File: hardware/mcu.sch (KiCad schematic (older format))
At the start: 22 parts, among them P3 SWD, P4 SPI3, P5 UART5, P7 USB_B, SW1 RESET, SW2 BOOT, U5 STM32F405R, U7 USBUFxxW6, X1 8MHz

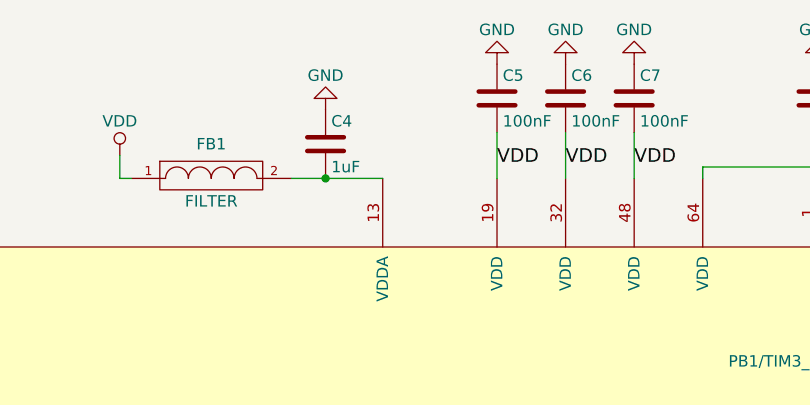
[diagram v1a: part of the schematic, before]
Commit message: Preliminary routing with LTC4417
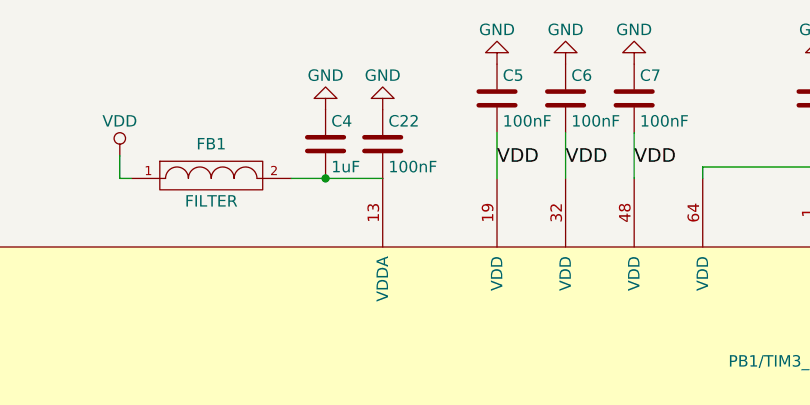
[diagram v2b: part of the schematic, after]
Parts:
- added C22: 100nF, Capacitors_SMD:C_0805, symbol C
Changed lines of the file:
@@
 EESchema Schematic File Version 2
+LIBS:rgb-matrix-rescue
 LIBS:power
 LIBS:device
@@
 $EndDescr
 $Comp
-L GND #PWR010
+L GND #PWR011
 U 1 1 580FD53D
 P 3800 5950
-F 0 "#PWR010" H 3800 5700 50  0001 C CNN
+F 0 "#PWR011" H 3800 5700 50  0001 C CNN
 F 1 "GND" H 3800 5800 50  0000 C CNN
 F 2 "" H 3800 5950 50  0000 C CNN
@@
 $EndComp
 $Comp
-L GND #PWR011
+L GND #PWR012
 U 1 1 580FFFC5
 P 4400 750
-F 0 "#PWR011" H 4400 500 50  0001 C CNN
+F 0 "#PWR012" H 4400 500 50  0001 C CNN
 F 1 "GND" H 4400 600 50  0000 C CNN
 F 2 "" H 4400 750 50  0000 C CNN
@@
 $EndComp
 $Comp
-L GND #PWR012
+L GND #PWR013
 U 1 1 58100274
 P 4700 750
-F 0 "#PWR012" H 4700 500 50  0001 C CNN
+F 0 "#PWR013" H 4700 500 50  0001 C CNN
 F 1 "GND" H 4700 600 50  0000 C CNN
 F 2 "" H 4700 750 50  0000 C CNN
@@
 $EndComp
 $Comp
-L GND #PWR013
+L GND #PWR014
 U 1 1 581002A9
 P 5000 750
-F 0 "#PWR013" H 5000 500 50  0001 C CNN
+F 0 "#PWR014" H 5000 500 50  0001 C CNN
 F 1 "GND" H 5000 600 50  0000 C CNN
 F 2 "" H 5000 750 50  0000 C CNN
@@
 $EndComp
 $Comp
-L GND #PWR014
+L GND #PWR015
 U 1 1 58100346
 P 5800 750
-F 0 "#PWR014" H 5800 500 50  0001 C CNN
+F 0 "#PWR015" H 5800 500 50  0001 C CNN
 F 1 "GND" H 5800 600 50  0000 C CNN
 F 2 "" H 5800 750 50  0000 C CNN
@@
 $EndComp
 $Comp
-L GND #PWR015
+L GND #PWR016
 U 1 1 58100502
 P 900 2450
-F 0 "#PWR015" H 900 2200 50  0001 C CNN
+F 0 "#PWR016" H 900 2200 50  0001 C CNN
 F 1 "GND" H 900 2300 50  0000 C CNN
 F 2 "" H 900 2450 50  0000 C CNN
@@
 $EndComp
 $Comp
-L GND #PWR016
+L GND #PWR017
 U 1 1 5810057A
 P 3650 950
-F 0 "#PWR016" H 3650 700 50  0001 C CNN
+F 0 "#PWR017" H 3650 700 50  0001 C CNN
 F 1 "GND" H 3650 800 50  0000 C CNN
 F 2 "" H 3650 950 50  0000 C CNN
@@
 $EndComp
 $Comp
-L VDD #PWR017
+L VDD #PWR018
 U 1 1 581006D5
 P 2750 1150
-F 0 "#PWR017" H 2750 1000 50  0001 C CNN
+F 0 "#PWR018" H 2750 1000 50  0001 C CNN
 F 1 "VDD" H 2750 1300 50  0000 C CNN
 F 2 "" H 2750 1150 50  0000 C CNN
@@
 $EndComp
 $Comp
-L GND #PWR018
+L GND #PWR019
 U 1 1 581008E0
 P 4000 5950
-F 0 "#PWR018" H 4000 5700 50  0001 C CNN
+F 0 "#PWR019" H 4000 5700 50  0001 C CNN
 F 1 "GND" H 4000 5800 50  0000 C CNN
 F 2 "" H 4000 5950 50  0000 C CNN
@@
 $EndComp
 $Comp
-L GND #PWR019
+L GND #PWR020
 U 1 1 58100906
 P 4200 5950
-F 0 "#PWR019" H 4200 5700 50  0001 C CNN
+F 0 "#PWR020" H 4200 5700 50  0001 C CNN
 F 1 "GND" H 4200 5800 50  0000 C CNN
 F 2 "" H 4200 5950 50  0000 C CNN
@@
 $EndComp
 $Comp
-L GND #PWR020
+L GND #PWR021
 U 1 1 58100A18
 P 5100 6250
-F 0 "#PWR020" H 5100 6000 50  0001 C CNN
+F 0 "#PWR021" H 5100 6000 50  0001 C CNN
 F 1 "GND" H 5100 6100 50  0000 C CNN
 F 2 "" H 5100 6250 50  0000 C CNN
@@
 $EndComp
 $Comp
-L GND #PWR021
+L GND #PWR022
 U 1 1 58100A9B
 P 5600 6250
-F 0 "#PWR021" H 5600 6000 50  0001 C CNN
+F 0 "#PWR022" H 5600 6000 50  0001 C CNN
 F 1 "GND" H 5600 6100 50  0000 C CNN
 F 2 "" H 5600 6250 50  0000 C CNN
@@
 $EndComp
 $Comp
-L GND #PWR022
+L GND #PWR023
 U 1 1 581010C3
 P 900 3050
-F 0 "#PWR022" H 900 2800 50  0001 C CNN
+F 0 "#PWR023" H 900 2800 50  0001 C CNN
 F 1 "GND" H 900 2900 50  0000 C CNN
 F 2 "" H 900 3050 50  0000 C CNN
@@
 NRST
 $Comp
-L GND #PWR023
+L GND #PWR024
 U 1 1 58102147
 P 1050 7500
-F 0 "#PWR023" H 1050 7250 50  0001 C CNN
+F 0 "#PWR024" H 1050 7250 50  0001 C CNN
 F 1 "GND" H 1050 7350 50  0000 C CNN
 F 2 "" H 1050 7500 50  0000 C CNN
@@
 BOOT1
 $Comp
-L GND #PWR024
+L GND #PWR025
 U 1 1 5815BDE6
 P 1950 7550
-F 0 "#PWR024" H 1950 7300 50  0001 C CNN
+F 0 "#PWR025" H 1950 7300 50  0001 C CNN
 F 1 "GND" H 1950 7400 50  0000 C CNN
 F 2 "" H 1950 7550 50  0000 C CNN
@@
 BOOT0
 $Comp
-L VDD #PWR025
+L VDD #PWR026
 U 1 1 5815C70B
 P 1950 6300
-F 0 "#PWR025" H 1950 6150 50  0001 C CNN
+F 0 "#PWR026" H 1950 6150 50  0001 C CNN
 F 1 "VDD" H 1950 6450 50  0000 C CNN
 F 2 "" H 1950 6300 50  0000 C CNN
@@
 $EndComp
 $Comp
-L VDD #PWR026
+L VDD #PWR027
 U 1 1 5815F752
 P 1050 6450
-F 0 "#PWR026" H 1050 6300 50  0001 C CNN
+F 0 "#PWR027" H 1050 6300 50  0001 C CNN
 F 1 "VDD" H 1050 6600 50  0000 C CNN
 F 2 "" H 1050 6450 50  0000 C CNN
@@
 SPI3_NSS
 $Comp
-L GND #PWR027
+L GND #PWR028
 U 1 1 581B0CAC
 P 10650 4600
-F 0 "#PWR027" H 10650 4350 50  0001 C CNN
+F 0 "#PWR028" H 10650 4350 50  0001 C CNN
 F 1 "GND" H 10650 4450 50  0000 C CNN
 F 2 "" H 10650 4600 50  0000 C CNN
@@
 $EndComp
 $Comp
-L +5V #PWR028
+L +5V #PWR029
 U 1 1 581B0D1D
 P 10650 4100
-F 0 "#PWR028" H 10650 3950 50  0001 C CNN
+F 0 "#PWR029" H 10650 3950 50  0001 C CNN
 F 1 "+5V" H 10650 4240 50  0000 C CNN
 F 2 "" H 10650 4100 50  0000 C CNN
@@
 $EndComp
 $Comp
-L GND #PWR029
+L GND #PWR030
 U 1 1 581C3953
 P 10650 5400
-F 0 "#PWR029" H 10650 5150 50  0001 C CNN
+F 0 "#PWR030" H 10650 5150 50  0001 C CNN
 F 1 "GND" H 10650 5250 50  0000 C CNN
 F 2 "" H 10650 5400 50  0000 C CNN
@@
 $EndComp
 $Comp
-L +5V #PWR030
+L +5V #PWR031
 U 1 1 581C3C79
 P 10200 5600
-F 0 "#PWR030" H 10200 5450 50  0001 C CNN
+F 0 "#PWR031" H 10200 5450 50  0001 C CNN
 F 1 "+5V" H 10200 5740 50  0000 C CNN
 F 2 "" H 10200 5600 50  0000 C CNN
@@
 $EndComp
 $Comp
-L GND #PWR031
+L GND #PWR032
 U 1 1 582B947A
 P 8650 1050
-F 0 "#PWR031" H 8650 800 50  0001 C CNN
+F 0 "#PWR032" H 8650 800 50  0001 C CNN
 F 1 "GND" H 8650 900 50  0000 C CNN
 F 2 "" H 8650 1050 50  0000 C CNN
@@
 U 1 1 582B9480
 P 10750 950
+AR Path="/582B9480" Ref="P7"  Part="1"
+AR Path="/580FBD10/582B9480" Ref="P7"  Part="1"
 F 0 "P7" V 10450 850 50  0000 C CNN
 F 1 "USB_B" H 10700 1150 50  0000 C CNN
@@
 $EndComp
 $Comp
-L GND #PWR032
+L GND #PWR033
 U 1 1 582B9487
 P 10450 1400
-F 0 "#PWR032" H 10450 1150 50  0001 C CNN
+F 0 "#PWR033" H 10450 1150 50  0001 C CNN
 F 1 "GND" H 10450 1250 50  0000 C CNN
 F 2 "" H 10450 1400 50  0000 C CNN
@@
 $EndComp
 $Comp
-L +3V3 #PWR033
+L +3V3 #PWR034
 U 1 1 582B948D
 P 10100 1050
-F 0 "#PWR033" H 10100 900 50  0001 C CNN
+F 0 "#PWR034" H 10100 900 50  0001 C CNN
 F 1 "+3V3" H 10100 1190 50  0000 C CNN
 F 2 "" H 10100 1050 50  0000 C CNN
@@
 	10850 1350 10450 1350
 Connection ~ 10450 1350
+$Comp
+L C C22
+U 1 1 587848A6
+P 3900 1100
+F 0 "C22" H 3925 1200 50  0000 L CNN
+F 1 "100nF" H 3925 1000 50  0000 L CNN
+F 2 "Capacitors_SMD:C_0805" H 3938 950 50  0001 C CNN
+F 3 "" H 3900 1100 50  0000 C CNN
+	1    3900 1100
+	1    0    0    -1
+$EndComp
+$Comp
+L GND #PWR035
+U 1 1 58784915
+P 3900 950
+F 0 "#PWR035" H 3900 700 50  0001 C CNN
+F 1 "GND" H 3900 800 50  0000 C CNN
+F 2 "" H 3900 950 50  0000 C CNN
+F 3 "" H 3900 950 50  0000 C CNN
+	1    3900 950
+	-1   0    0    1
+$EndComp
 $EndSCHEMATC

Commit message: Fix silkscreen
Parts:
- C1, C10, C11, C2, C22, C3, C4, C5, C6, C7, C8: footprint Capacitors_SMD:C_0805 -> rgb-matrix:C_0805
- FB1, R26, R27: footprint Resistors_SMD:R_0805 -> rgb-matrix:R_0805
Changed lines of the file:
@@
 F 0 "C5" H 4425 1000 50  0000 L CNN
 F 1 "100nF" H 4425 800 50  0000 L CNN
-F 2 "Capacitors_SMD:C_0805" H 4438 750 50  0001 C CNN
+F 2 "rgb-matrix:C_0805" H 4438 750 50  0001 C CNN
 F 3 "" H 4400 900 50  0000 C CNN
 	1    4400 900
@@
 F 0 "C6" H 4725 1000 50  0000 L CNN
 F 1 "100nF" H 4725 800 50  0000 L CNN
-F 2 "Capacitors_SMD:C_0805" H 4738 750 50  0001 C CNN
+F 2 "rgb-matrix:C_0805" H 4738 750 50  0001 C CNN
 F 3 "" H 4700 900 50  0000 C CNN
 	1    4700 900
@@
 F 0 "C7" H 5025 1000 50  0000 L CNN
 F 1 "100nF" H 5025 800 50  0000 L CNN
-F 2 "Capacitors_SMD:C_0805" H 5038 750 50  0001 C CNN
+F 2 "rgb-matrix:C_0805" H 5038 750 50  0001 C CNN
 F 3 "" H 5000 900 50  0000 C CNN
 	1    5000 900
@@
 F 0 "C11" H 5825 1000 50  0000 L CNN
 F 1 "100nF" H 5825 800 50  0000 L CNN
-F 2 "Capacitors_SMD:C_0805" H 5838 750 50  0001 C CNN
+F 2 "rgb-matrix:C_0805" H 5838 750 50  0001 C CNN
 F 3 "" H 5800 900 50  0000 C CNN
 	1    5800 900
@@
 F 0 "C2" H 1075 2550 50  0000 L CNN
 F 1 "18pF" H 1075 2350 50  0000 L CNN
-F 2 "Capacitors_SMD:C_0805" H 1088 2300 50  0001 C CNN
+F 2 "rgb-matrix:C_0805" H 1088 2300 50  0001 C CNN
 F 3 "" H 1050 2450 50  0000 C CNN
 	1    1050 2450
@@
 F 0 "C4" H 3675 1200 50  0000 L CNN
 F 1 "1uF" H 3675 1000 50  0000 L CNN
-F 2 "Capacitors_SMD:C_0805" H 3688 950 50  0001 C CNN
+F 2 "rgb-matrix:C_0805" H 3688 950 50  0001 C CNN
 F 3 "" H 3650 1100 50  0000 C CNN
 	1    3650 1100
@@
 F 0 "FB1" H 3150 1400 50  0000 C CNN
 F 1 "FILTER" H 3150 1150 50  0000 C CNN
-F 2 "Resistors_SMD:R_0805" H 3150 1250 50  0001 C CNN
+F 2 "rgb-matrix:R_0805" H 3150 1250 50  0001 C CNN
 F 3 "" H 3150 1250 50  0000 C CNN
 	1    3150 1250
@@
 F 0 "C8" H 5125 6200 50  0000 L CNN
 F 1 "2.2uF" H 5125 6000 50  0000 L CNN
-F 2 "Capacitors_SMD:C_0805" H 5138 5950 50  0001 C CNN
+F 2 "rgb-matrix:C_0805" H 5138 5950 50  0001 C CNN
 F 3 "" H 5100 6100 50  0000 C CNN
 	1    5100 6100
@@
 F 0 "C10" H 5625 6200 50  0000 L CNN
 F 1 "2.2uF" H 5625 6000 50  0000 L CNN
-F 2 "Capacitors_SMD:C_0805" H 5638 5950 50  0001 C CNN
+F 2 "rgb-matrix:C_0805" H 5638 5950 50  0001 C CNN
 F 3 "" H 5600 6100 50  0000 C CNN
 	1    5600 6100
@@
 F 0 "C3" H 1075 3150 50  0000 L CNN
 F 1 "18pF" H 1075 2950 50  0000 L CNN
-F 2 "Capacitors_SMD:C_0805" H 1088 2900 50  0001 C CNN
+F 2 "rgb-matrix:C_0805" H 1088 2900 50  0001 C CNN
 F 3 "" H 1050 3050 50  0000 C CNN
 	1    1050 3050
@@
 F 0 "R27" V 2030 7250 50  0000 C CNN
 F 1 "10k" V 1950 7250 50  0000 C CNN
-F 2 "Resistors_SMD:R_0805" V 1880 7250 50  0001 C CNN
+F 2 "rgb-matrix:R_0805" V 1880 7250 50  0001 C CNN
 F 3 "" H 1950 7250 50  0000 C CNN
 	1    1950 7250
@@
 F 0 "C1" H 925 7250 50  0000 L CNN
 F 1 "100nF" H 925 7050 50  0000 L CNN
-F 2 "Capacitors_SMD:C_0805" H 938 7000 50  0001 C CNN
+F 2 "rgb-matrix:C_0805" H 938 7000 50  0001 C CNN
 F 3 "" H 900 7150 50  0000 C CNN
 	1    900  7150
@@
 F 0 "R26" V 1130 6650 50  0000 C CNN
 F 1 "10k" V 1050 6650 50  0000 C CNN
-F 2 "Resistors_SMD:R_0805" V 980 6650 50  0001 C CNN
+F 2 "rgb-matrix:R_0805" V 980 6650 50  0001 C CNN
 F 3 "" H 1050 6650 50  0000 C CNN
 	1    1050 6650
@@
 Text GLabel 1200 4750 0    60   UnSpc ~ 0
 VBUS
-Wire Wire Line
-	8200 2150 8600 2150
-Wire Wire Line
-	1200 5050 600  5050
-Wire Wire Line
-	1200 4950 600  4950
-Wire Wire Line
-	8200 2250 8600 2250
-Wire Wire Line
-	1200 5150 600  5150
-Wire Wire Line
-	1200 5250 600  5250
-Wire Wire Line
-	10650 3400 10050 3400
-Wire Wire Line
-	10650 3300 10050 3300
-Wire Wire Line
-	10650 3200 10050 3200
-Wire Wire Line
-	10650 3100 10050 3100
-Wire Wire Line
-	10650 3000 10050 3000
-Wire Wire Line
-	10650 2900 10050 2900
-Wire Wire Line
-	1200 2900 1200 3050
-Wire Wire Line
-	1200 2450 1200 2600
-Wire Wire Line
-	900  7000 900  6850
-Connection ~ 1050 7450
-Wire Wire Line
-	900  7450 900  7300
-Wire Wire Line
-	1050 7450 1050 7500
-Wire Wire Line
-	900  7450 1200 7450
-Wire Wire Line
-	850  2250 1200 2250
-Wire Wire Line
-	850  2050 1200 2050
-Connection ~ 3650 1250
-Wire Wire Line
-	3500 1250 3900 1250
-Wire Wire Line
-	5800 1050 5800 1250
-Wire Wire Line
-	5000 1050 5000 1250
-Wire Wire Line
-	4700 1050 4700 1250
-Wire Wire Line
-	4400 1050 4400 1250
-Wire Wire Line
-	1600 7050 1950 7050
-Wire Wire Line
-	1950 6950 1950 7100
-Wire Wire Line
-	1950 6300 1950 6350
-Connection ~ 1950 7050
-Wire Wire Line
-	1050 6450 1050 6500
-Wire Wire Line
-	650  6850 1200 6850
-Connection ~ 900  6850
-Wire Wire Line
-	1050 6850 1050 6800
-Connection ~ 1050 6850
-Wire Wire Line
-	1950 7400 1950 7550
-Wire Wire Line
-	1600 7500 1950 7500
-Connection ~ 1950 7500
-Wire Wire Line
-	2750 1150 2750 1250
-Wire Wire Line
-	2750 1250 2800 1250
-Wire Wire Line
-	1200 4450 1200 4450
-Wire Wire Line
-	1200 4550 1200 4550
-Wire Wire Line
-	8200 4750 8700 4750
-Wire Wire Line
-	8200 4850 8700 4850
-Wire Wire Line
-	8200 4950 9250 4950
-Wire Wire Line
-	600  5350 1200 5350
-Wire Wire Line
-	10650 4200 10200 4200
-Wire Wire Line
-	10200 4300 10650 4300
-Wire Wire Line
-	10200 4400 10650 4400
-Wire Wire Line
-	10200 4500 10650 4500
-Wire Wire Line
-	750  3450 1200 3450
-Wire Wire Line
-	10650 5700 10200 5700
-Wire Wire Line
-	10200 5800 10650 5800
-Wire Wire Line
-	10200 5600 10650 5600
-Wire Wire Line
-	5800 1200 5300 1200
-Wire Wire Line
-	5300 1200 5300 1250
-Connection ~ 5800 1200
 Text Label 8700 1150 0    60   ~ 0
 USB_DM
@@
 VBUS
 NoConn ~ 10450 1050
-Wire Wire Line
-	10200 750  10450 750
-Wire Wire Line
-	10100 950  10450 950
-Wire Wire Line
-	10350 850  10450 850
-Wire Wire Line
-	10350 1150 10350 850
-Wire Wire Line
-	10350 1150 10100 1150
-Wire Wire Line
-	8650 1050 9100 1050
-Wire Wire Line
-	9100 950  8700 950
-Wire Wire Line
-	9100 1150 8700 1150
-Wire Wire Line
-	10450 1150 10450 1400
-Wire Wire Line
-	10850 1350 10450 1350
-Connection ~ 10450 1350
 $Comp
 L C C22
@@
 F 0 "C22" H 3925 1200 50  0000 L CNN
 F 1 "100nF" H 3925 1000 50  0000 L CNN
-F 2 "Capacitors_SMD:C_0805" H 3938 950 50  0001 C CNN
+F 2 "rgb-matrix:C_0805" H 3938 950 50  0001 C CNN
 F 3 "" H 3900 1100 50  0000 C CNN
 	1    3900 1100
@@
 	-1   0    0    1
 $EndComp
+Wire Wire Line
+	8200 2150 8600 2150
+Wire Wire Line
+	1200 5050 600  5050
+Wire Wire Line
+	1200 4950 600  4950
+Wire Wire Line
+	8200 2250 8600 2250
+Wire Wire Line
+	1200 5150 600  5150
+Wire Wire Line
+	1200 5250 600  5250
+Wire Wire Line
+	10650 3400 10050 3400
+Wire Wire Line
+	10650 3300 10050 3300
+Wire Wire Line
+	10650 3200 10050 3200
+Wire Wire Line
+	10650 3100 10050 3100
+Wire Wire Line
+	10650 3000 10050 3000
+Wire Wire Line
+	10650 2900 10050 2900
+Wire Wire Line
+	1200 2900 1200 3050
+Wire Wire Line
+	1200 2450 1200 2600
+Wire Wire Line
+	900  7000 900  6850
+Connection ~ 1050 7450
+Wire Wire Line
+	900  7450 900  7300
+Wire Wire Line
+	1050 7450 1050 7500
+Wire Wire Line
+	900  7450 1200 7450
+Wire Wire Line
+	850  2250 1200 2250
+Wire Wire Line
+	850  2050 1200 2050
+Connection ~ 3650 1250
+Wire Wire Line
+	3500 1250 3900 1250
+Wire Wire Line
+	5800 1050 5800 1250
+Wire Wire Line
+	5000 1050 5000 1250
+Wire Wire Line
+	4700 1050 4700 1250
+Wire Wire Line
+	4400 1050 4400 1250
+Wire Wire Line
+	1600 7050 1950 7050
+Wire Wire Line
+	1950 6950 1950 7100
+Wire Wire Line
+	1950 6300 1950 6350
+Connection ~ 1950 7050
+Wire Wire Line
+	1050 6450 1050 6500
+Wire Wire Line
+	650  6850 1200 6850
+Connection ~ 900  6850
+Wire Wire Line
+	1050 6850 1050 6800
+Connection ~ 1050 6850
+Wire Wire Line
+	1950 7400 1950 7550
+Wire Wire Line
+	1600 7500 1950 7500
+Connection ~ 1950 7500
+Wire Wire Line
+	2750 1150 2750 1250
+Wire Wire Line
+	2750 1250 2800 1250
+Wire Wire Line
+	1200 4450 1200 4450
+Wire Wire Line
+	1200 4550 1200 4550
+Wire Wire Line
+	8200 4750 8700 4750
+Wire Wire Line
+	8200 4850 8700 4850
+Wire Wire Line
+	8200 4950 9250 4950
+Wire Wire Line
+	600  5350 1200 5350
+Wire Wire Line
+	10650 4200 10200 4200
+Wire Wire Line
+	10200 4300 10650 4300
+Wire Wire Line
+	10200 4400 10650 4400
+Wire Wire Line
+	10200 4500 10650 4500
+Wire Wire Line
+	750  3450 1200 3450
+Wire Wire Line
+	10650 5700 10200 5700
+Wire Wire Line
+	10200 5800 10650 5800
+Wire Wire Line
+	10200 5600 10650 5600
+Wire Wire Line
+	5800 1200 5300 1200
+Wire Wire Line
+	5300 1200 5300 1250
+Connection ~ 5800 1200
+Wire Wire Line
+	10200 750  10450 750
+Wire Wire Line
+	10100 950  10450 950
+Wire Wire Line
+	10350 850  10450 850
+Wire Wire Line
+	10350 1150 10350 850
+Wire Wire Line
+	10350 1150 10100 1150
+Wire Wire Line
+	8650 1050 9100 1050
+Wire Wire Line
+	9100 950  8700 950
+Wire Wire Line
+	9100 1150 8700 1150
+Wire Wire Line
+	10450 1150 10450 1400
+Wire Wire Line
+	10850 1350 10450 1350
+Connection ~ 10450 1350
 $EndSCHEMATC

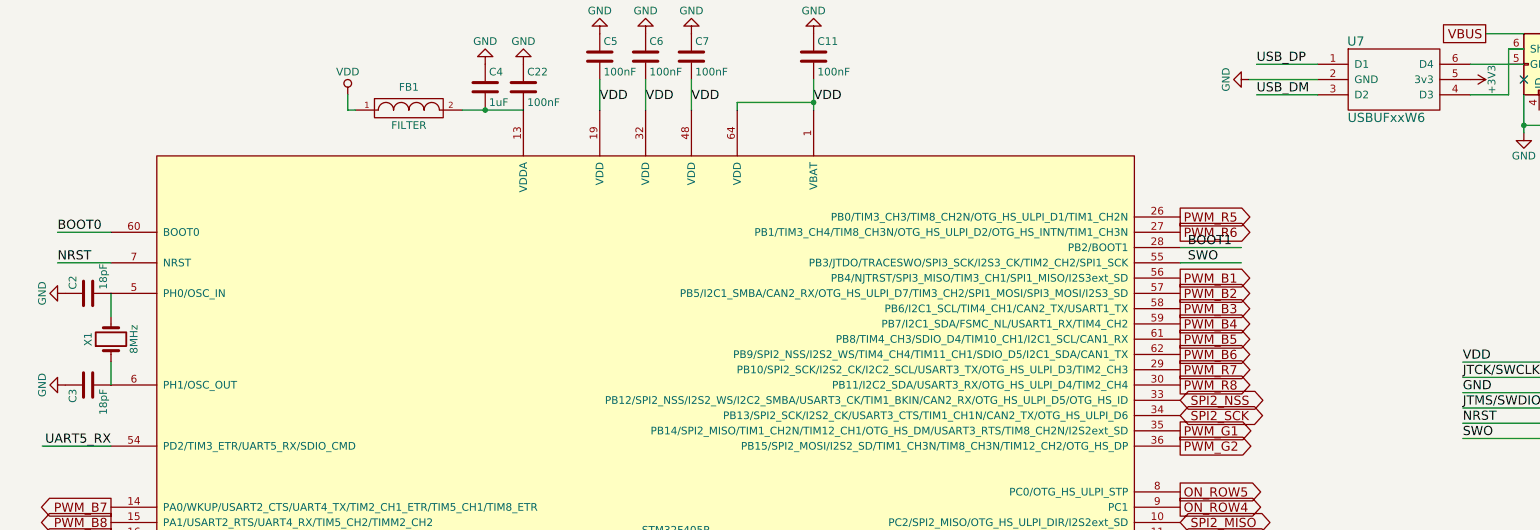
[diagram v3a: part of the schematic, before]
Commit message: Add 2nd GND pin for more curent + minor changes
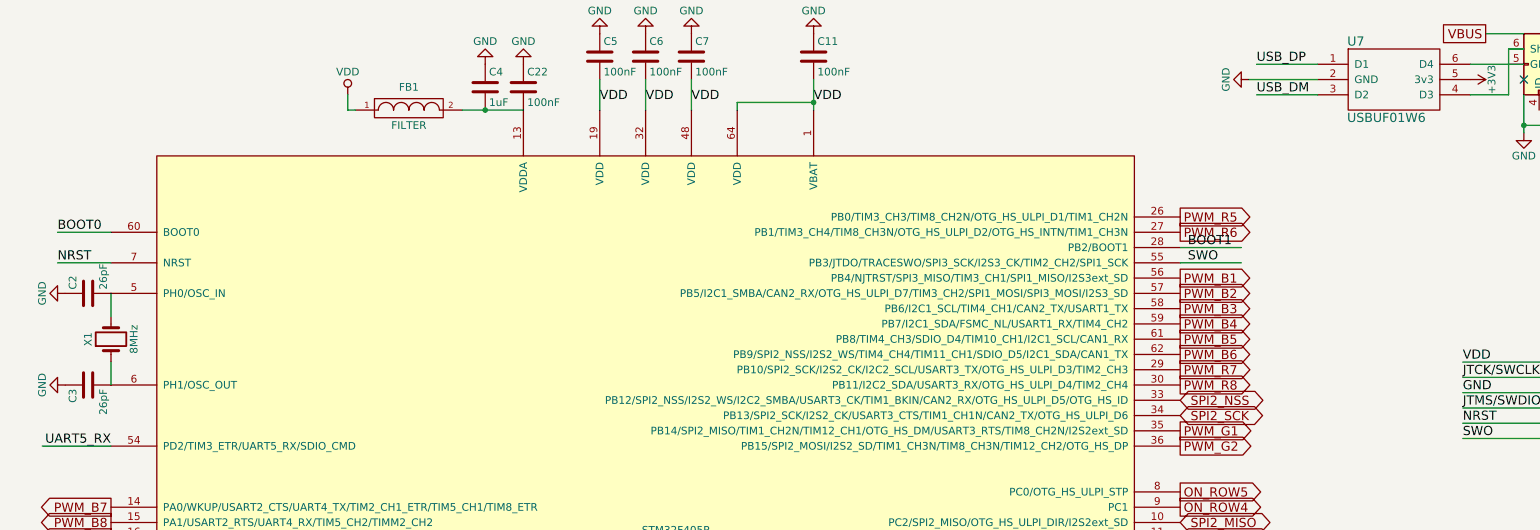
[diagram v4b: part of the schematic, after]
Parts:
- C2, C3: value 18pF -> 26pF
- U7: value USBUFxxW6 -> USBUF01W6
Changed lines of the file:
@@
 P 1050 2450
 F 0 "C2" H 1075 2550 50  0000 L CNN
-F 1 "18pF" H 1075 2350 50  0000 L CNN
+F 1 "26pF" H 1075 2350 50  0000 L CNN
 F 2 "rgb-matrix:C_0805" H 1088 2300 50  0001 C CNN
 F 3 "" H 1050 2450 50  0000 C CNN
@@
 P 1050 3050
 F 0 "C3" H 1075 3150 50  0000 L CNN
-F 1 "18pF" H 1075 2950 50  0000 L CNN
+F 1 "26pF" H 1075 2950 50  0000 L CNN
 F 2 "rgb-matrix:C_0805" H 1088 2900 50  0001 C CNN
 F 3 "" H 1050 3050 50  0000 C CNN
@@
 P 9600 1050
 F 0 "U7" H 9350 1300 60  0000 C CNN
-F 1 "USBUFxxW6" H 9550 800 60  0000 C CNN
+F 1 "USBUF01W6" H 9550 800 60  0000 C CNN
 F 2 "TO_SOT_Packages_SMD:SC-70-6" H 9600 1350 60  0001 C CNN
 F 3 "" H 9600 1350 60  0001 C CNN

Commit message: Fix footprint for U7, minor other fixes
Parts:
- U7: footprint TO_SOT_Packages_SMD:SC-70-6 -> rgb-matrix:SOT323-6L
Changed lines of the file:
@@
 F 0 "U7" H 9350 1300 60  0000 C CNN
 F 1 "USBUF01W6" H 9550 800 60  0000 C CNN
-F 2 "TO_SOT_Packages_SMD:SC-70-6" H 9600 1350 60  0001 C CNN
+F 2 "rgb-matrix:SOT323-6L" H 9600 1350 60  0001 C CNN
 F 3 "" H 9600 1350 60  0001 C CNN
 	1    9600 1050

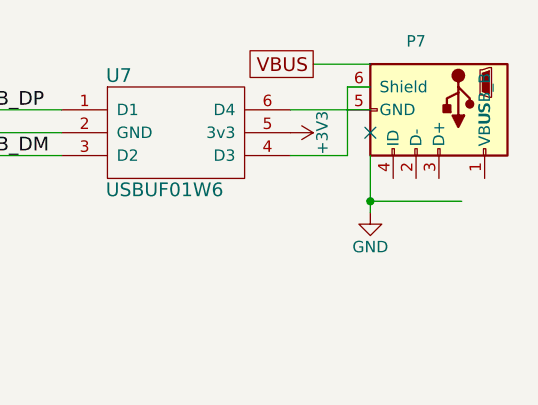
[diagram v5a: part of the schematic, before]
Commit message: Update component versions (ULN2308A and USB_B)
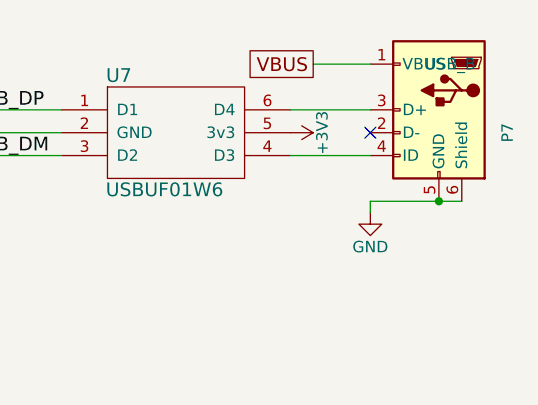
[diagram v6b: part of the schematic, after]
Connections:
- wire segments 61 -> 59
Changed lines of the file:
@@
 F 3 "" V 10700 850 50  0000 C CNN
 	1    10750 950
-	0    1    1    0
+	-1   0    0    -1
 $EndComp
 $Comp
@@
 	10100 950  10450 950
 Wire Wire Line
-	10350 850  10450 850
-Wire Wire Line
-	10350 1150 10350 850
-Wire Wire Line
-	10350 1150 10100 1150
+	10100 1150 10450 1150
 Wire Wire Line
 	8650 1050 9100 1050
@@
 	9100 1150 8700 1150
 Wire Wire Line
-	10450 1150 10450 1400
+	10450 1350 10450 1400
 Wire Wire Line
-	10850 1350 10450 1350
-Connection ~ 10450 1350
+	10450 1350 10850 1350
+Connection ~ 10750 1350
 $EndSCHEMATC
